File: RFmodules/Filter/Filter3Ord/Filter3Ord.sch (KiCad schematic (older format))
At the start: 8 parts, among them J1 SMA, J2 SMA

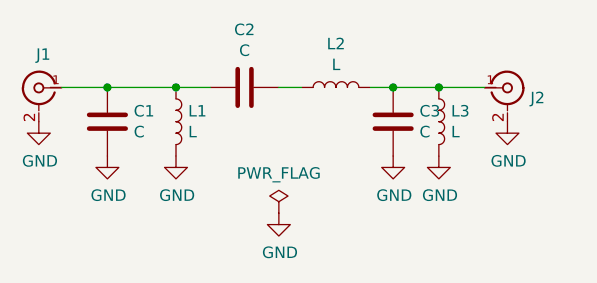
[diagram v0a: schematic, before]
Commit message: Add bandpass filter 3 order 0402
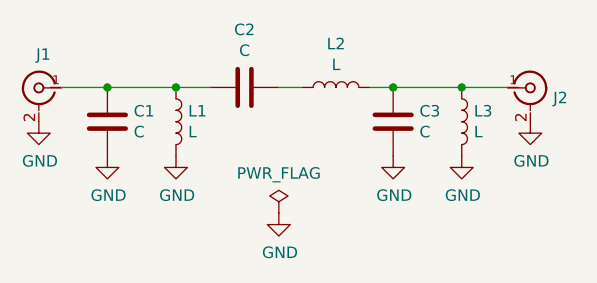
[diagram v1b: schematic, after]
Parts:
- C1, C2, C3: footprint Capacitor_SMD:C_1206_3216Metric_Pad1.42x1.75mm_HandSolder -> Capacitor_SMD:C_0402_1005Metric
- L1, L2, L3: footprint Inductor_SMD:L_1206_3216Metric_Pad1.42x1.75mm_HandSolder -> Inductor_SMD:L_0402_1005Metric
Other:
- moved on the sheet: J2, L3
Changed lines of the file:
@@
 EESchema Schematic File Version 4
+LIBS:Filter3Ord-cache
 EELAYER 26 0
 EELAYER END
@@
 L RFLego_Schematic:SMA J2
 U 1 1 5C17E84A
-P 4050 3050
-F 0 "J2" H 4150 3004 50  0000 L CNN
-F 1 "SMA" H 4170 2790 50  0001 C CNN
-F 2 "RFLego_Footprint:SMA_Edge" H 4050 2748 50  0001 C CNN
-F 3 "" H 4050 2748 50  0001 C CNN
-	1    4050 3050
+P 4150 3050
+F 0 "J2" H 4250 3004 50  0000 L CNN
+F 1 "SMA" H 4270 2790 50  0001 C CNN
+F 2 "RFLego_Footprint:SMA_Edge" H 4150 2748 50  0001 C CNN
+F 3 "" H 4150 2748 50  0001 C CNN
+	1    4150 3050
 	1    0    0    -1
 $EndComp
@@
 F 0 "L1" H 2653 3246 50  0000 L CNN
 F 1 "L" H 2653 3155 50  0000 L CNN
-F 2 "Inductor_SMD:L_1206_3216Metric_Pad1.42x1.75mm_HandSolder" H 2600 3200 50  0001 C CNN
+F 2 "Inductor_SMD:L_0402_1005Metric" H 2600 3200 50  0001 C CNN
 F 3 "~" H 2600 3200 50  0001 C CNN
 	1    2600 3200
@@
 L Device:L L3
 U 1 1 5C17EA40
-P 3750 3200
-F 0 "L3" H 3803 3246 50  0000 L CNN
-F 1 "L" H 3803 3155 50  0000 L CNN
-F 2 "Inductor_SMD:L_1206_3216Metric_Pad1.42x1.75mm_HandSolder" H 3750 3200 50  0001 C CNN
-F 3 "~" H 3750 3200 50  0001 C CNN
-	1    3750 3200
+P 3850 3200
+F 0 "L3" H 3903 3246 50  0000 L CNN
+F 1 "L" H 3903 3155 50  0000 L CNN
+F 2 "Inductor_SMD:L_0402_1005Metric" H 3850 3200 50  0001 C CNN
+F 3 "~" H 3850 3200 50  0001 C CNN
+	1    3850 3200
 	1    0    0    -1
 $EndComp
@@
 F 0 "L2" V 3490 3050 50  0000 C CNN
 F 1 "L" V 3399 3050 50  0000 C CNN
-F 2 "Inductor_SMD:L_1206_3216Metric_Pad1.42x1.75mm_HandSolder" H 3300 3050 50  0001 C CNN
+F 2 "Inductor_SMD:L_0402_1005Metric" H 3300 3050 50  0001 C CNN
 F 3 "~" H 3300 3050 50  0001 C CNN
 	1    3300 3050
@@
 F 0 "C1" H 2415 3246 50  0000 L CNN
 F 1 "C" H 2415 3155 50  0000 L CNN
-F 2 "Capacitor_SMD:C_1206_3216Metric_Pad1.42x1.75mm_HandSolder" H 2338 3050 50  0001 C CNN
+F 2 "Capacitor_SMD:C_0402_1005Metric" H 2338 3050 50  0001 C CNN
 F 3 "~" H 2300 3200 50  0001 C CNN
 	1    2300 3200
@@
 F 0 "C2" V 2648 3050 50  0000 C CNN
 F 1 "C" V 2739 3050 50  0000 C CNN
-F 2 "Capacitor_SMD:C_1206_3216Metric_Pad1.42x1.75mm_HandSolder" H 2938 2900 50  0001 C CNN
+F 2 "Capacitor_SMD:C_0402_1005Metric" H 2938 2900 50  0001 C CNN
 F 3 "~" H 2900 3050 50  0001 C CNN
 	1    2900 3050
@@
 F 0 "C3" H 3665 3246 50  0000 L CNN
 F 1 "C" H 3665 3155 50  0000 L CNN
-F 2 "Capacitor_SMD:C_1206_3216Metric_Pad1.42x1.75mm_HandSolder" H 3588 3050 50  0001 C CNN
+F 2 "Capacitor_SMD:C_0402_1005Metric" H 3588 3050 50  0001 C CNN
 F 3 "~" H 3550 3200 50  0001 C CNN
 	1    3550 3200
@@
 L power:GND #PWR06
 U 1 1 5C17EEE8
-P 3750 3350
-F 0 "#PWR06" H 3750 3100 50  0001 C CNN
-F 1 "GND" H 3755 3177 50  0000 C CNN
-F 2 "" H 3750 3350 50  0001 C CNN
-F 3 "" H 3750 3350 50  0001 C CNN
-	1    3750 3350
+P 3850 3350
+F 0 "#PWR06" H 3850 3100 50  0001 C CNN
+F 1 "GND" H 3855 3177 50  0000 C CNN
+F 2 "" H 3850 3350 50  0001 C CNN
+F 3 "" H 3850 3350 50  0001 C CNN
+	1    3850 3350
 	1    0    0    -1
 $EndComp
@@
 L power:GND #PWR07
 U 1 1 5C17EF03
-P 4050 3200
-F 0 "#PWR07" H 4050 2950 50  0001 C CNN
-F 1 "GND" H 4055 3027 50  0000 C CNN
-F 2 "" H 4050 3200 50  0001 C CNN
-F 3 "" H 4050 3200 50  0001 C CNN
-	1    4050 3200
+P 4150 3200
+F 0 "#PWR07" H 4150 2950 50  0001 C CNN
+F 1 "GND" H 4155 3027 50  0000 C CNN
+F 2 "" H 4150 3200 50  0001 C CNN
+F 3 "" H 4150 3200 50  0001 C CNN
+	1    4150 3200
 	1    0    0    -1
 $EndComp
@@
 Wire Wire Line
 	3450 3050 3550 3050
-Wire Wire Line
-	3550 3050 3750 3050
-Connection ~ 3550 3050
-Wire Wire Line
-	3750 3050 3950 3050
-Connection ~ 3750 3050
 $Comp
 L power:PWR_FLAG #FLG01
@@
 	1    0    0    -1
 $EndComp
+Wire Wire Line
+	3550 3050 3850 3050
+Connection ~ 3550 3050
+Wire Wire Line
+	3850 3050 4050 3050
+Connection ~ 3850 3050
 $EndSCHEMATC
